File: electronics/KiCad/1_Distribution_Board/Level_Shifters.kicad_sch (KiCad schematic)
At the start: 26 parts, among them J101 Conn_01x04, J21 Generic 2.54mm, J22 Generic 2.54mm, J23 Generic 2.54mm, J24 Generic 2.54mm, J25 Generic 2.54mm, J26 Generic 2.54mm, J601 Conn_01x04, Q2 TBD, Q3 TBD

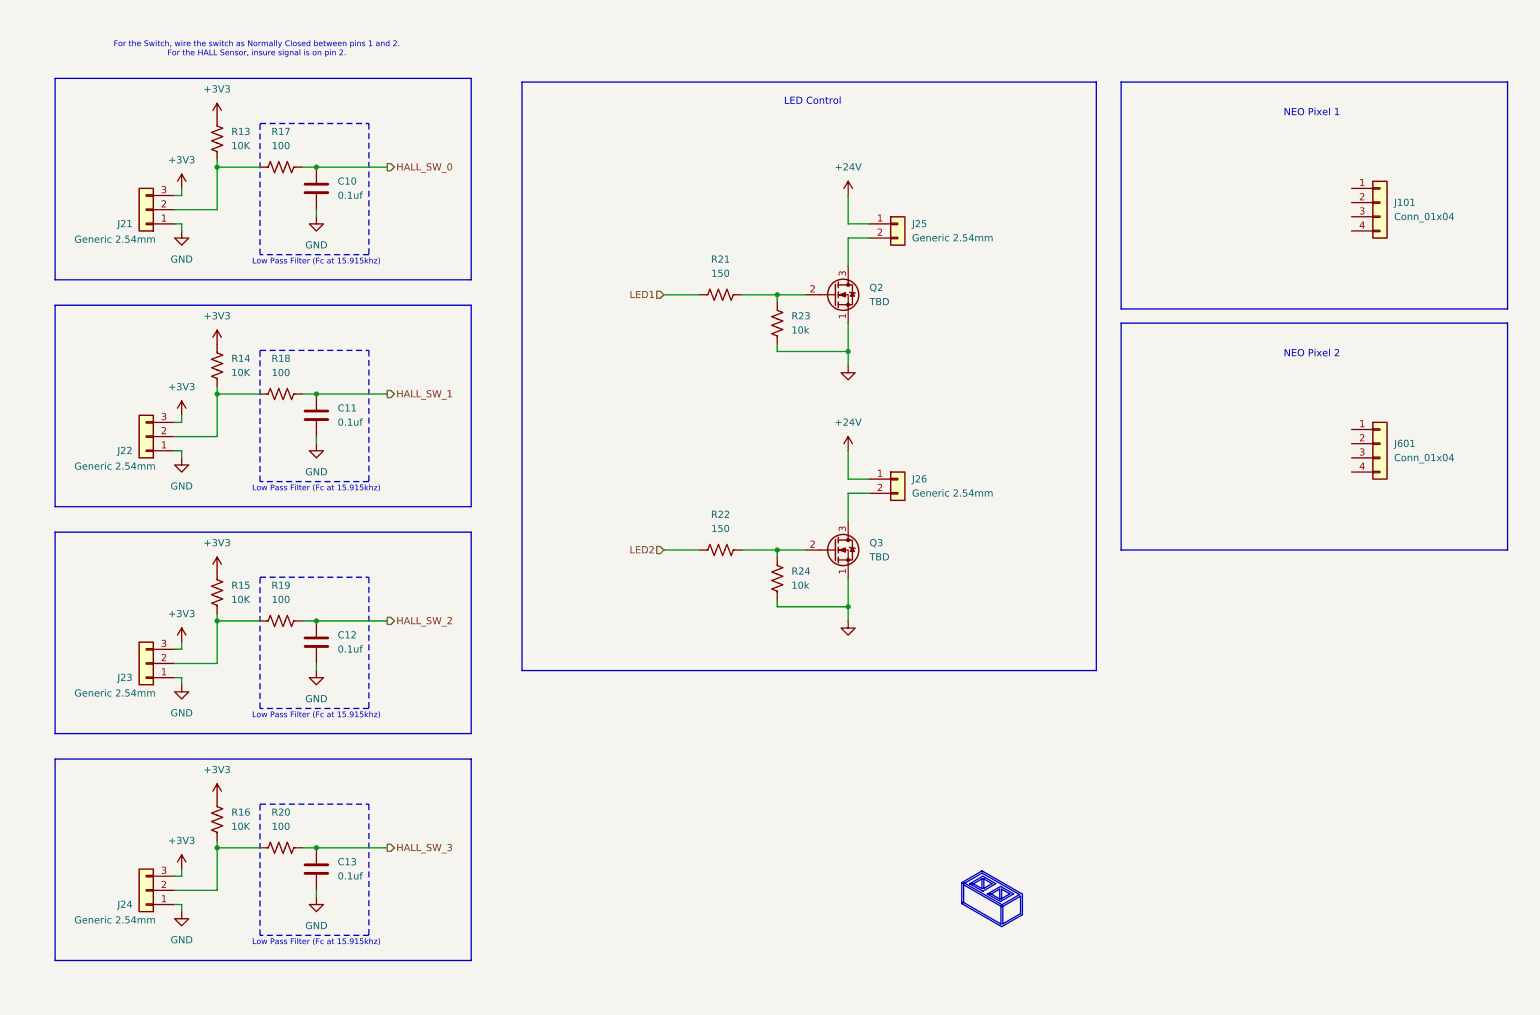
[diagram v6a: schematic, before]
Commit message: PCB updates
Added stepper module headers and working on silk for ease of debug.
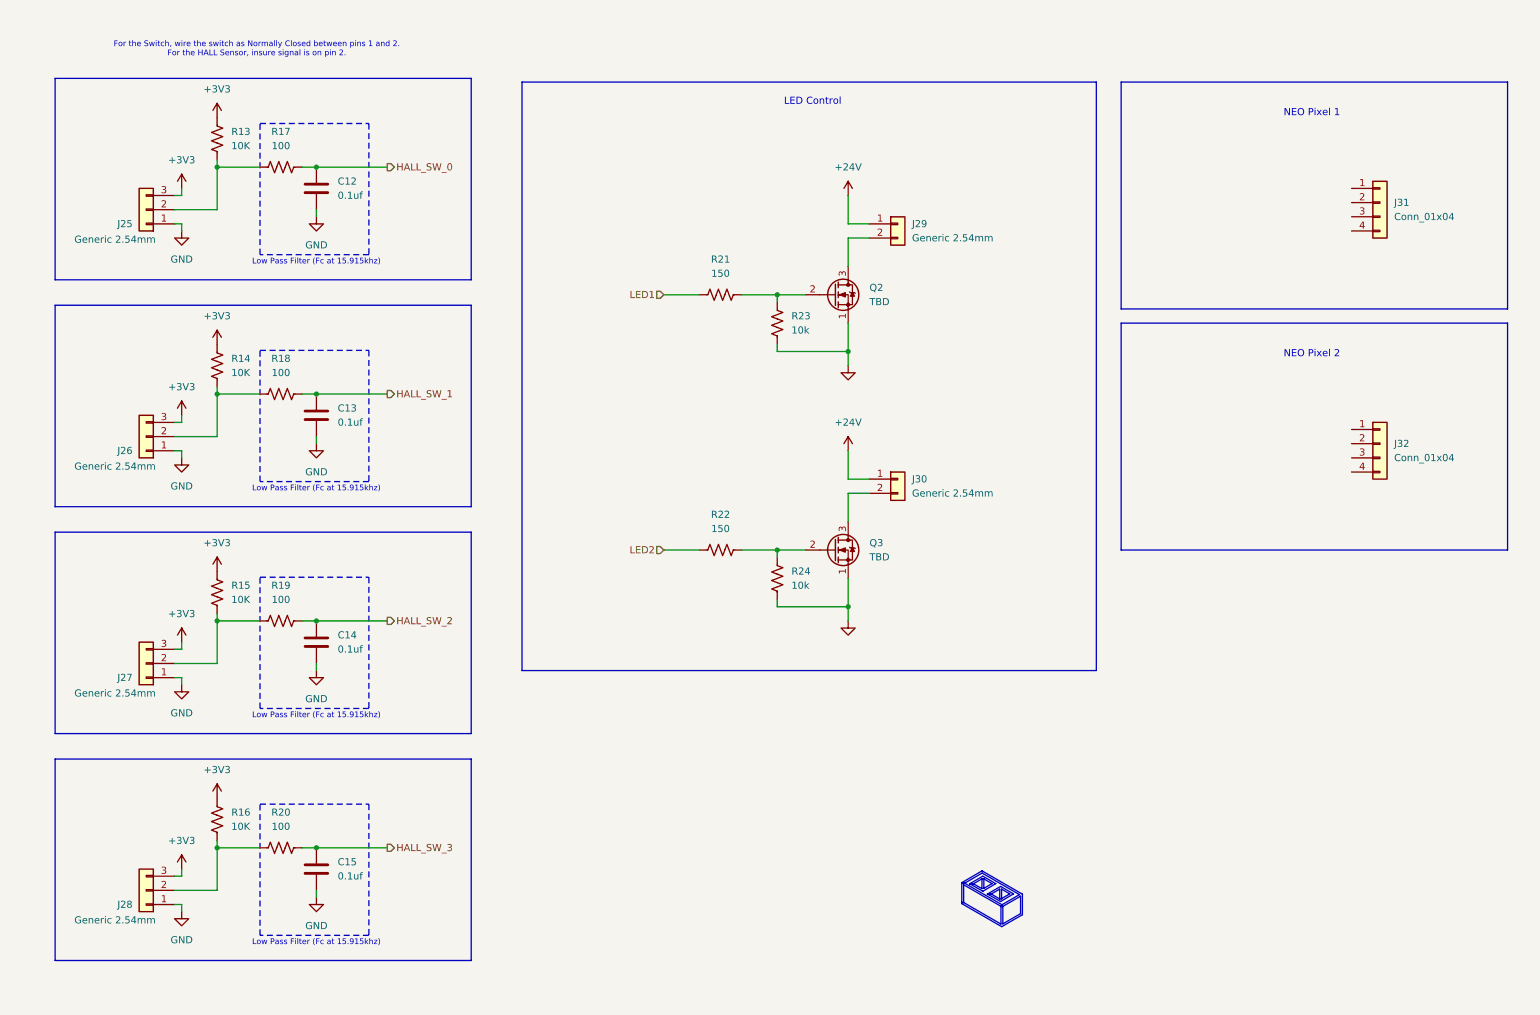
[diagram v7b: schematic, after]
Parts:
- renumbered C10 to C12, C11 to C13, C12 to C14, C13 to C15, J21 to J25, J22 to J26, J23 to J27, J24 to J28, J25 to J29, J26 to J30, J101 to J31, J601 to J32

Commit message: Updated PCB/SCH
Updated stepper schematics and motor schematics for clarity. Updated motor module to use headers. Updated stepper driver top be the BIGTREETECH V1.3. Cleaned up layout locations a bit.
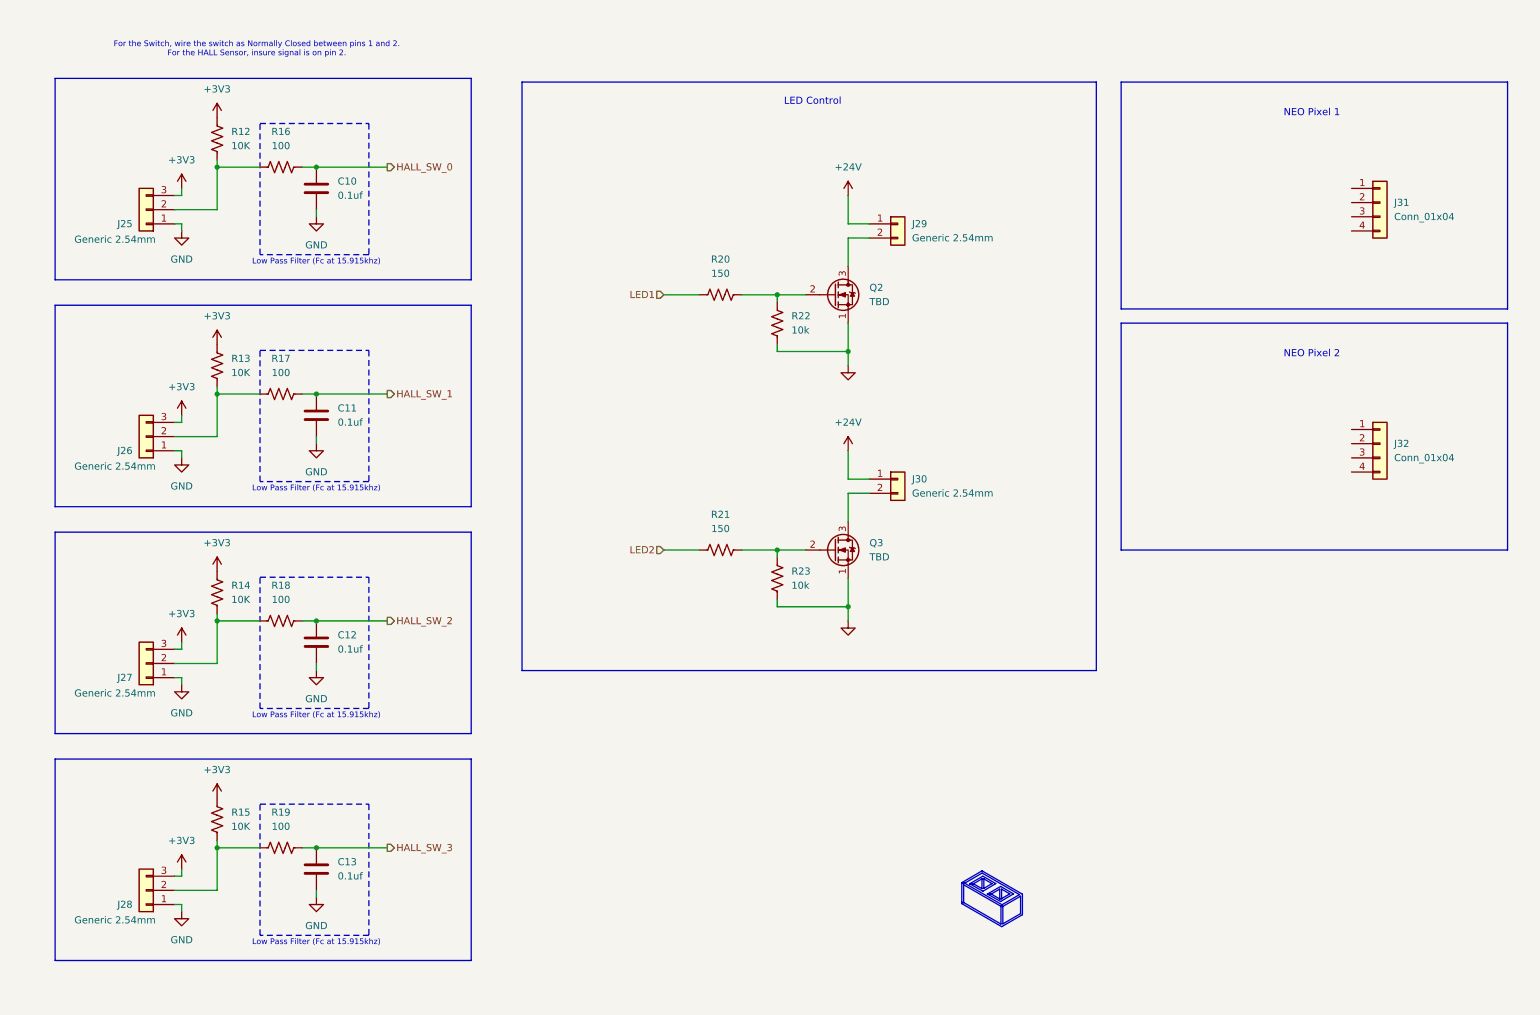
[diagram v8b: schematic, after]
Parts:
- renumbered C12 to C10, C13 to C11, C14 to C12, C15 to C13, R13 to R12, R14 to R13, R15 to R14, R16 to R15, R17 to R16, R18 to R17, R19 to R18, R20 to R19, R21 to R20, R22 to R21, R23 to R22, R24 to R23
